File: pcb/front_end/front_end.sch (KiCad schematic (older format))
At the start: 45 parts, among them J1 SMA, J10 SMA, J11 SMA, J12 SMA, J13 SMA, J14 SMA, J15 SMA, J16 SMA, J17 SMA, J18 SMA, J19 SMA, J2 SMA, J20 SMA, J21 SMA, J22 SMA, J23 SMA, J24 SMA, J25 SMA, J26 SMA, J27 SMA, J28 SMA, J29 SMA, J3 SMA, J30 SMA, J31 SMA, J4 SMA, J5 SMA, J6 SMA, J7 SMP, J8 SMP, J9 SMA

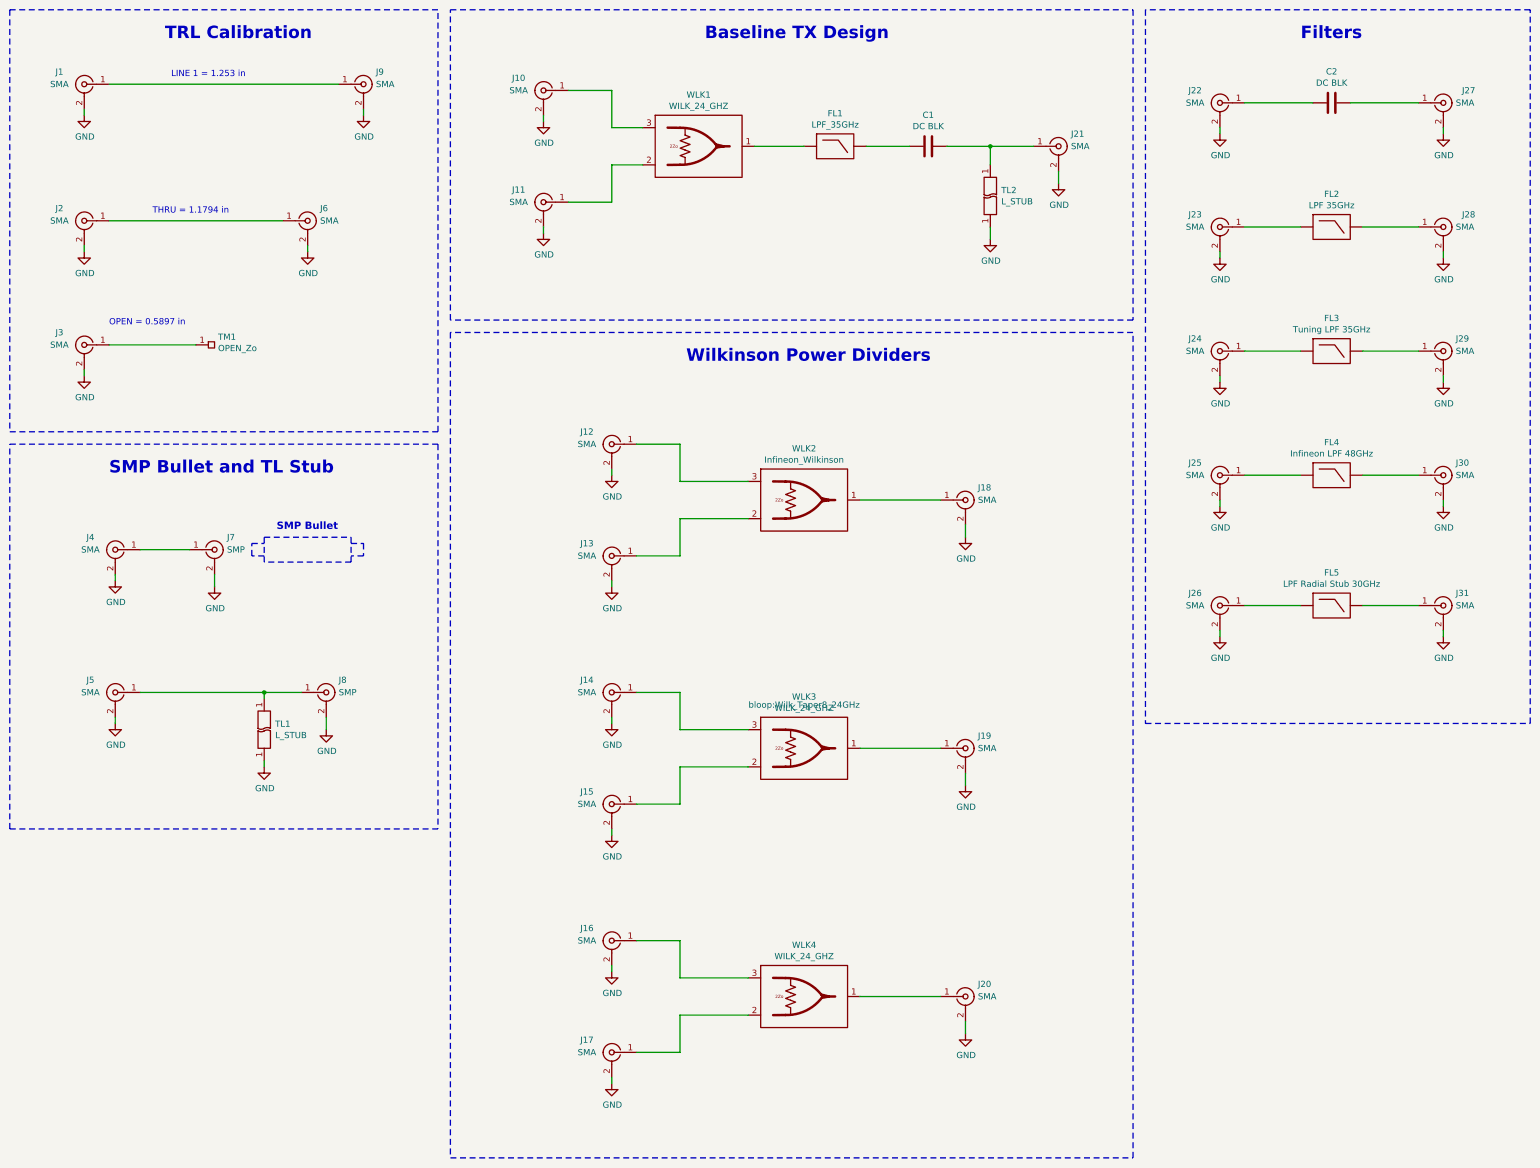
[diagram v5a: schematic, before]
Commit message: Removed matching stubs from front end schematic
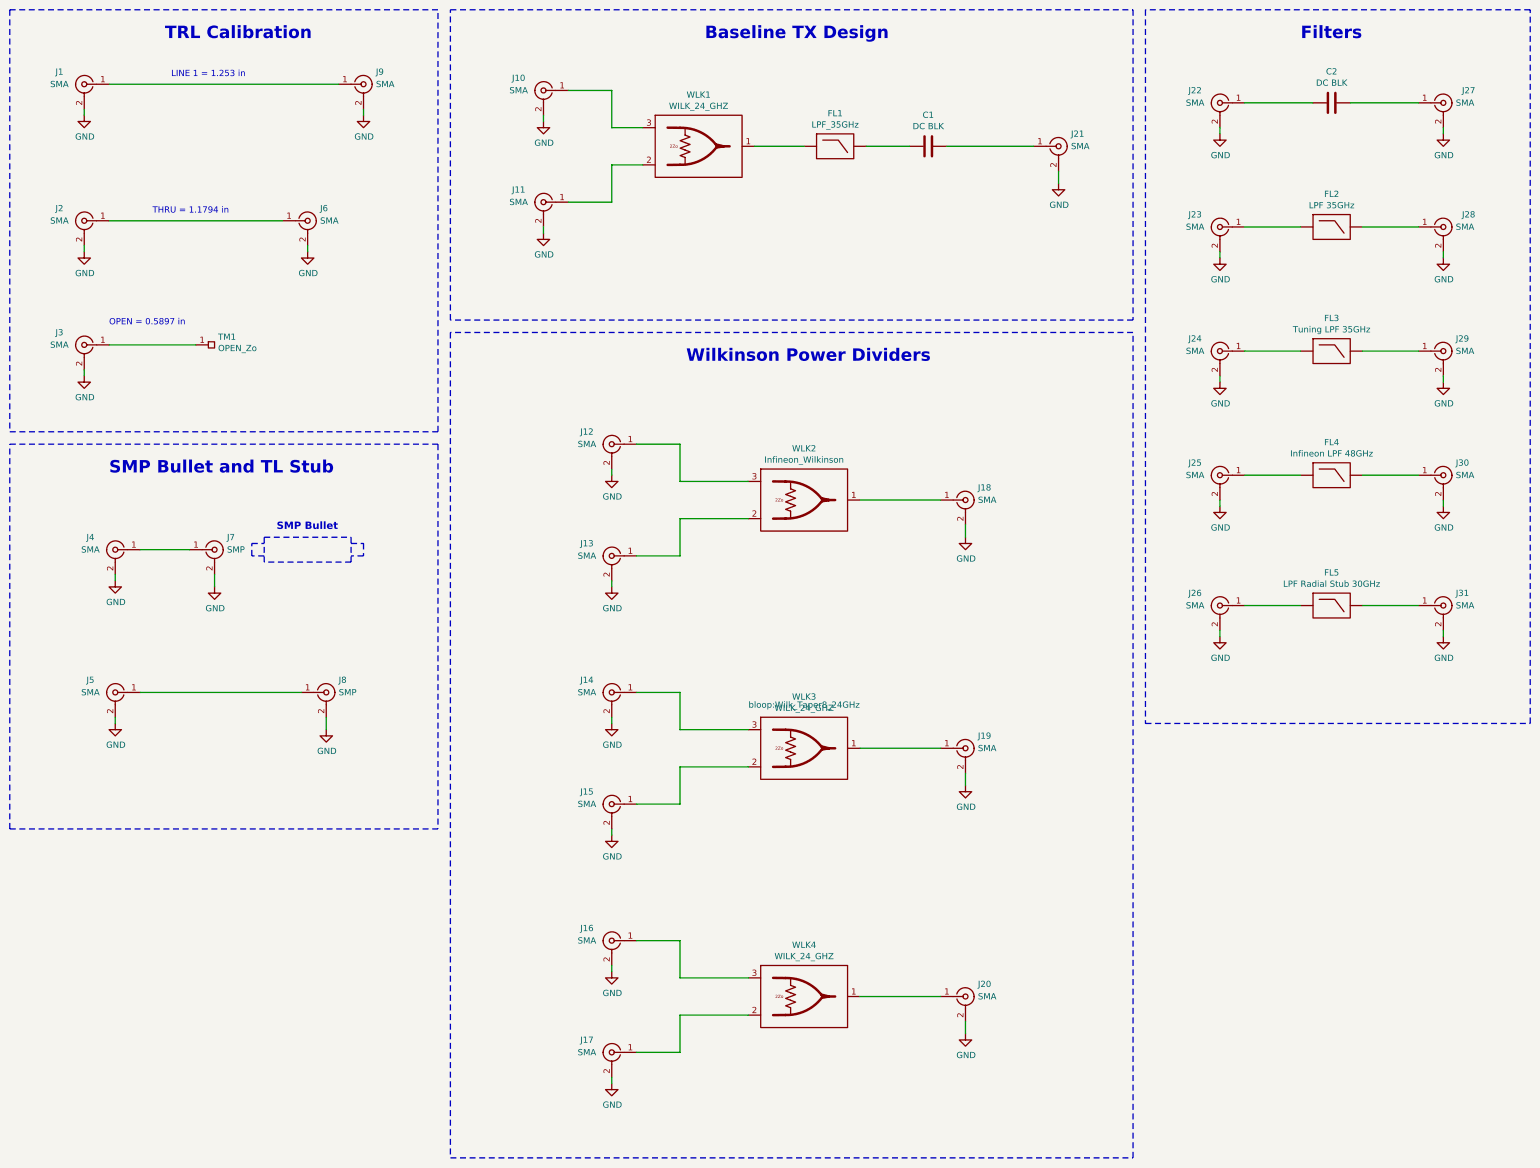
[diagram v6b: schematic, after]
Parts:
- removed TL1, TL2: L_STUB, symbol bloop:L_STUB
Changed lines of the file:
@@
 $EndComp
-Wire Wire Line
-	10500 1850 10500 2000
-Wire Wire Line
-	10500 2500 10500 2600
-$Comp
-L power:GND #PWR0102
-U 1 1 5D4A0E16
-P 10500 2600
-F 0 "#PWR0102" H 10500 2350 50  0001 C CNN
-F 1 "GND" H 10505 2427 50  0000 C CNN
-F 2 "" H 10500 2600 50  0001 C CNN
-F 3 "" H 10500 2600 50  0001 C CNN
-	1    10500 2600
-	1    0    0    -1
-$EndComp
-Wire Wire Line
-	10500 1850 10850 1850
 Wire Wire Line
 	14150 1700 14150 1750
@@
 	1    11050 1850
 	1    0    0    -1
-$EndComp
-$Comp
-L bloop:L_STUB TL2
-U 1 1 5D4914E7
-P 10500 2250
-F 0 "TL2" V 10454 2338 50  0000 L CNN
-F 1 "L_STUB" V 10545 2338 50  0000 L CNN
-F 2 "" H 10500 2400 50  0001 C CNN
-F 3 "" H 10500 2400 50  0001 C CNN
-F 4 "N/A" H 10500 2250 50  0001 C CNN "MPN"
-	1    10500 2250
-	0    1    1    0
 $EndComp
 $Comp
@@
 	-1   0    0    -1
 $EndComp
-Connection ~ 4650 6250
-Wire Wire Line
-	4950 6250 4650 6250
 $Comp
 L Connector:Conn_Coaxial J8
@@
 Wire Wire Line
 	5150 6450 5150 6550
-Wire Wire Line
-	4650 6250 4650 6300
-Wire Wire Line
-	3650 6250 4650 6250
 $Comp
 L power:GND #PWR0120
@@
 	-1   0    0    -1
 $EndComp
-Wire Wire Line
-	4650 6800 4650 6850
-$Comp
-L power:GND #PWR0121
-U 1 1 5D51D06E
-P 4650 6850
-F 0 "#PWR0121" H 4650 6600 50  0001 C CNN
-F 1 "GND" H 4655 6677 50  0000 C CNN
-F 2 "" H 4650 6850 50  0001 C CNN
-F 3 "" H 4650 6850 50  0001 C CNN
-	1    4650 6850
-	1    0    0    -1
-$EndComp
-$Comp
-L bloop:L_STUB TL1
-U 1 1 5D51C37E
-P 4650 6550
-F 0 "TL1" V 4604 6638 50  0000 L CNN
-F 1 "L_STUB" V 4695 6638 50  0000 L CNN
-F 2 "" H 4650 6700 50  0001 C CNN
-F 3 "" H 4650 6700 50  0001 C CNN
-F 4 "N/A" H 4650 6550 50  0001 C CNN "MPN"
-	1    4650 6550
-	0    1    1    0
-$EndComp
 $Comp
 L Connector:Conn_Coaxial J24
@@
 	9850 1850 9500 1850
 Wire Wire Line
-	10150 1850 10500 1850
-Connection ~ 10500 1850
-Wire Wire Line
 	3650 5100 4050 5100
 Wire Wire Line
 	11050 2050 11050 2150
+Wire Wire Line
+	3650 6250 4950 6250
+Wire Wire Line
+	10150 1850 10850 1850
 $EndSCHEMATC

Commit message: Generated Fabrication files
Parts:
- added C3: DC BLK, Capacitor_SMD:C_0402_1005Metric, symbol Device:C
- added J32, J33: SMA, bloop:292-06A-5, symbol Connector:Conn_Coaxial
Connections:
- net GND: now also J32.2 (Ext), J33.2 (Ext)
- new net: C3.1, J33.1 (In)
- new net: C3.2, J32.1 (In)
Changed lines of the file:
@@
 	14150 4700 14150 4750
 Wire Notes Line
-	11750 750  11750 6500
-Wire Notes Line
-	14850 6500 14850 750
+	11750 750  11750 7300
+Wire Notes Line
+	14850 7300 14850 750
 Wire Notes Line
 	14850 750  11750 750
@@
 SMP Bullet and TL Stub
 Wire Notes Line
-	11750 6500 14850 6500
+	11750 7300 14850 7300
 $Comp
 L Connector:Conn_Coaxial J31
@@
 Wire Wire Line
 	10150 1850 10850 1850
+Wire Wire Line
+	14150 6700 14150 6750
+$Comp
+L power:GND #PWR?
+U 1 1 5D80B028
+P 14150 6750
+F 0 "#PWR?" H 14150 6500 50  0001 C CNN
+F 1 "GND" H 14155 6577 50  0000 C CNN
+F 2 "" H 14150 6750 50  0001 C CNN
+F 3 "" H 14150 6750 50  0001 C CNN
+	1    14150 6750
+	1    0    0    -1
+$EndComp
+Wire Wire Line
+	13400 6500 13950 6500
+$Comp
+L power:GND #PWR?
+U 1 1 5D80B02F
+P 12350 6750
+F 0 "#PWR?" H 12350 6500 50  0001 C CNN
+F 1 "GND" H 12355 6577 50  0000 C CNN
+F 2 "" H 12350 6750 50  0001 C CNN
+F 3 "" H 12350 6750 50  0001 C CNN
+	1    12350 6750
+	1    0    0    -1
+$EndComp
+Wire Wire Line
+	12350 6700 12350 6750
+Wire Wire Line
+	13100 6500 12550 6500
+$Comp
+L Connector:Conn_Coaxial J33
+U 1 1 5D80B038
+P 14150 6500
+F 0 "J33" H 14300 6600 50  0000 L CNN
+F 1 "SMA" H 14250 6500 50  0000 L CNN
+F 2 "bloop:292-06A-5" H 14150 6500 50  0001 C CNN
+F 3 "https://www.hasco-inc.com/content/Southwest/End%20Launch/Jack/SMA_jack_endlaunch_genoutline.pdf" H 14150 6500 50  0001 C CNN
+F 4 "292-06A-5" H 14150 6500 50  0001 C CNN "MPN"
+	1    14150 6500
+	1    0    0    -1
+$EndComp
+$Comp
+L Connector:Conn_Coaxial J32
+U 1 1 5D80B03F
+P 12350 6500
+F 0 "J32" H 12550 6600 50  0000 C CNN
+F 1 "SMA" H 12550 6500 50  0000 C CNN
+F 2 "bloop:292-06A-5" H 12350 6500 50  0001 C CNN
+F 3 "https://www.hasco-inc.com/content/Southwest/End%20Launch/Jack/SMA_jack_endlaunch_genoutline.pdf" H 12350 6500 50  0001 C CNN
+F 4 "292-06A-5" H 12350 6500 50  0001 C CNN "MPN"
+	1    12350 6500
+	-1   0    0    -1
+$EndComp
+$Comp
+L Device:C C3
+U 1 1 5D80B045
+P 13250 6500
+F 0 "C3" V 12998 6500 50  0000 C CNN
+F 1 "DC BLK" V 13089 6500 50  0000 C CNN
+F 2 "Capacitor_SMD:C_0402_1005Metric" H 13288 6350 50  0001 C CNN
+F 3 "~" H 13250 6500 50  0001 C CNN
+	1    13250 6500
+	0    1    1    0
+$EndComp
 $EndSCHEMATC
